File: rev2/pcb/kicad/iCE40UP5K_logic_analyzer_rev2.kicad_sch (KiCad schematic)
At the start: 151 parts, among them IC1 ICE40UP5K-SG48I, IC2 MIC5504-3.3YM5-TR, IC3 MIC5504-1.2YM5-TR, IC4 FT2232HL-TRAY, IC5 W25Q40CLSNIG, IC6 SN74LVC14ADBRE4, IC7 SN74LVC14ADBRE4, IC8 SN74LVC14ADBRE4, J1 USB B Female Connector, J2 61300611121, J3 61202021621, J4 61300821121, J5 61300821121, Q1 2N7002H6327XTSA2, Y1 830208214809

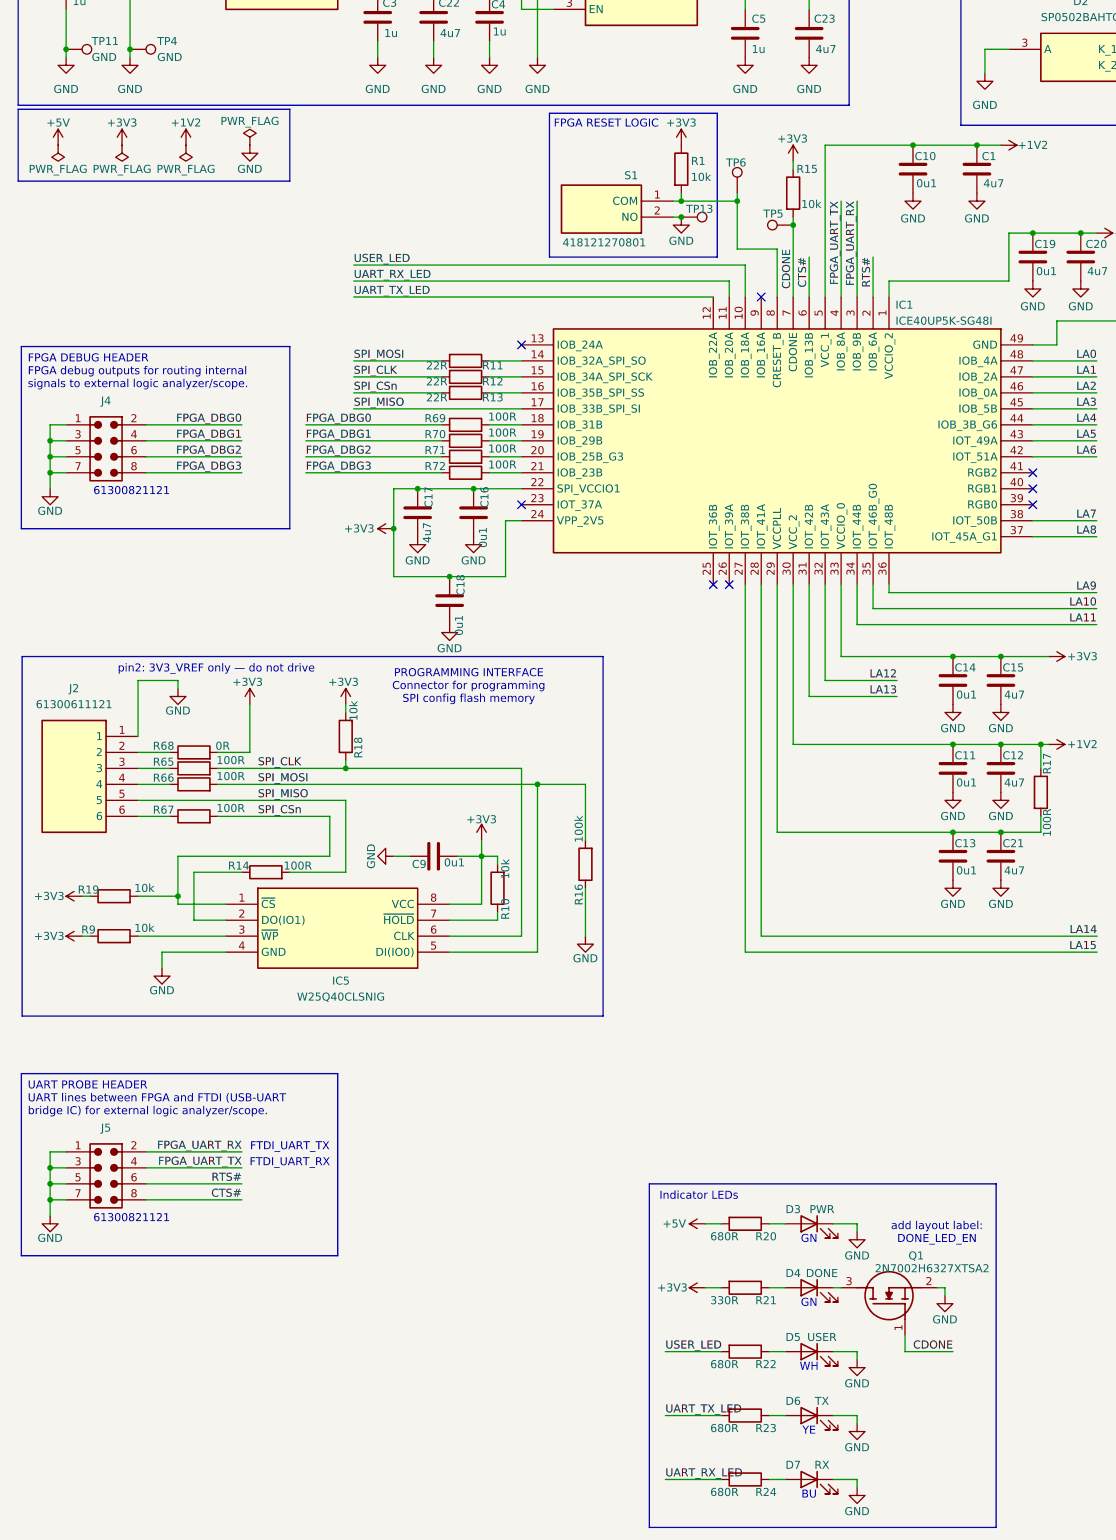
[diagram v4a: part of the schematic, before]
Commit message: Added CONFIG PROBE HEADER to schematic.
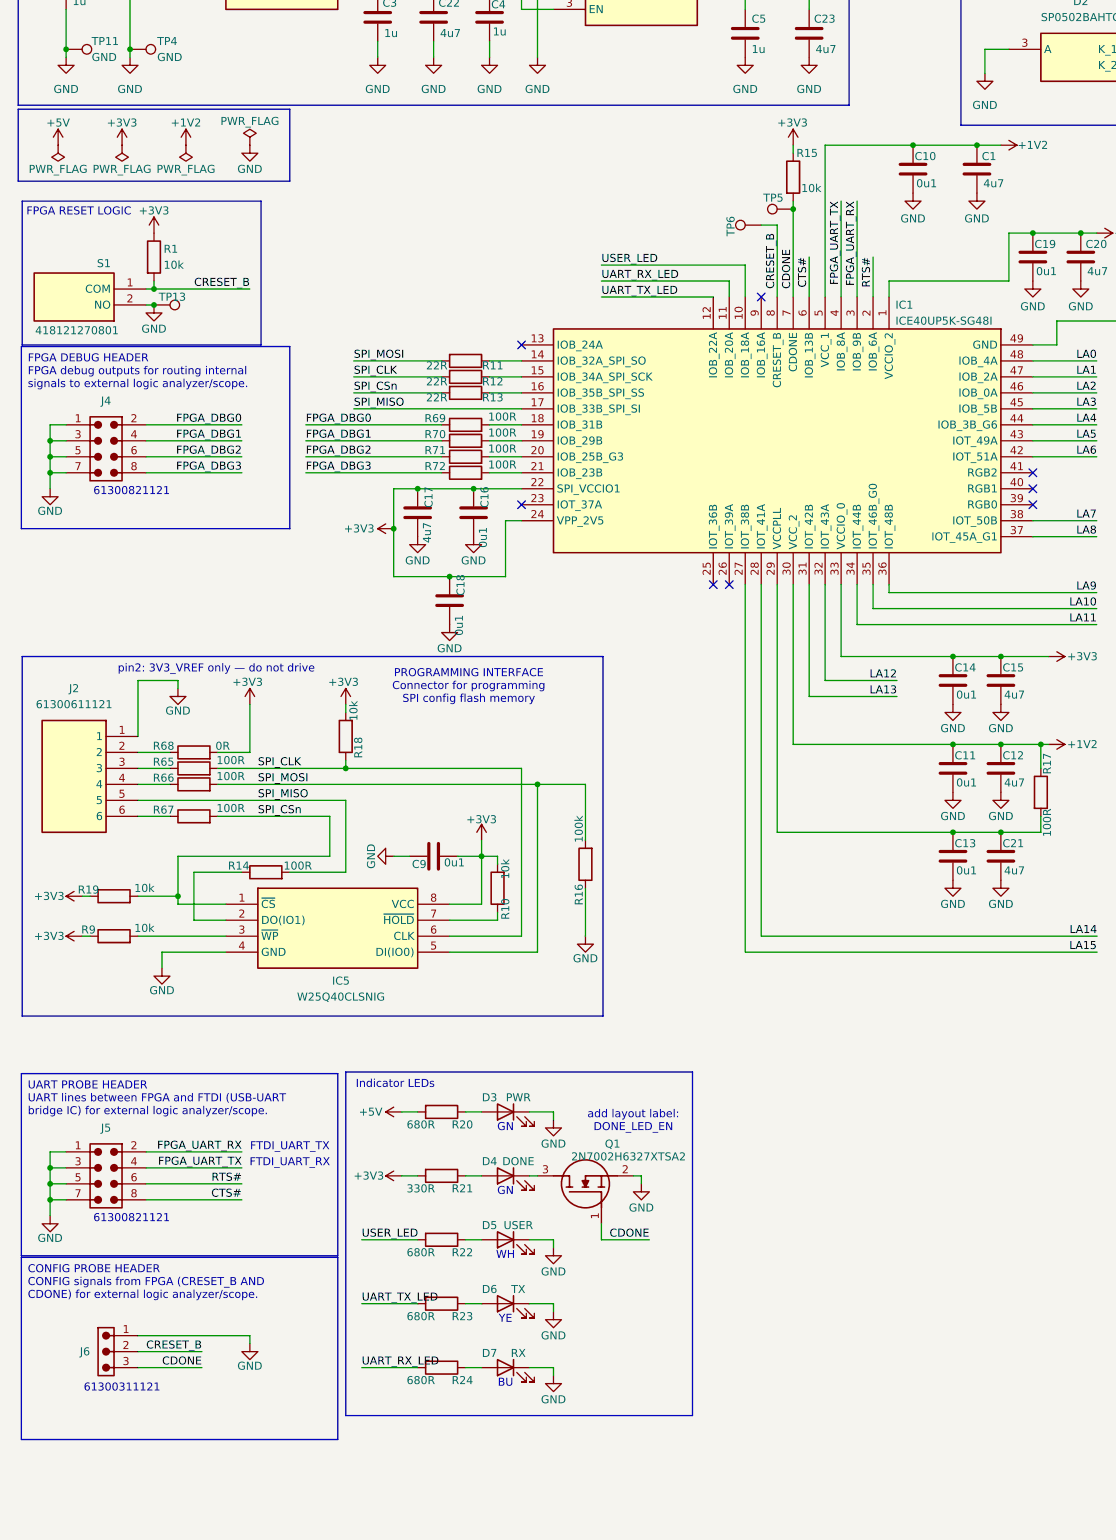
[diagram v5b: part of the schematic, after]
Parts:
- added J6: 61300311121, Connector_THT_Wurth:J_Wurth_WR-PHD_61300311121, symbol 8_pin_2x4_61300821121:61300311121
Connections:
- net CDONE: now also J6.3
- net GND: now also J6.1
- net CRESET_B: now reaches IC1.8 (CRESET_B), R1.2, S1.1 (COM), TP6.1
- net CRESET_B: now also J6.2
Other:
- note added: "61300311121"
- note added: "CONFIG PROBE HEADER CONFIG signals from FPGA (CRESET_B AND CDONE) for external logic analyzer/scope."
- moved on the sheet: D3, D4, D5, D6, D7, Q1, R1, R15, R20, R21, R22, R23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

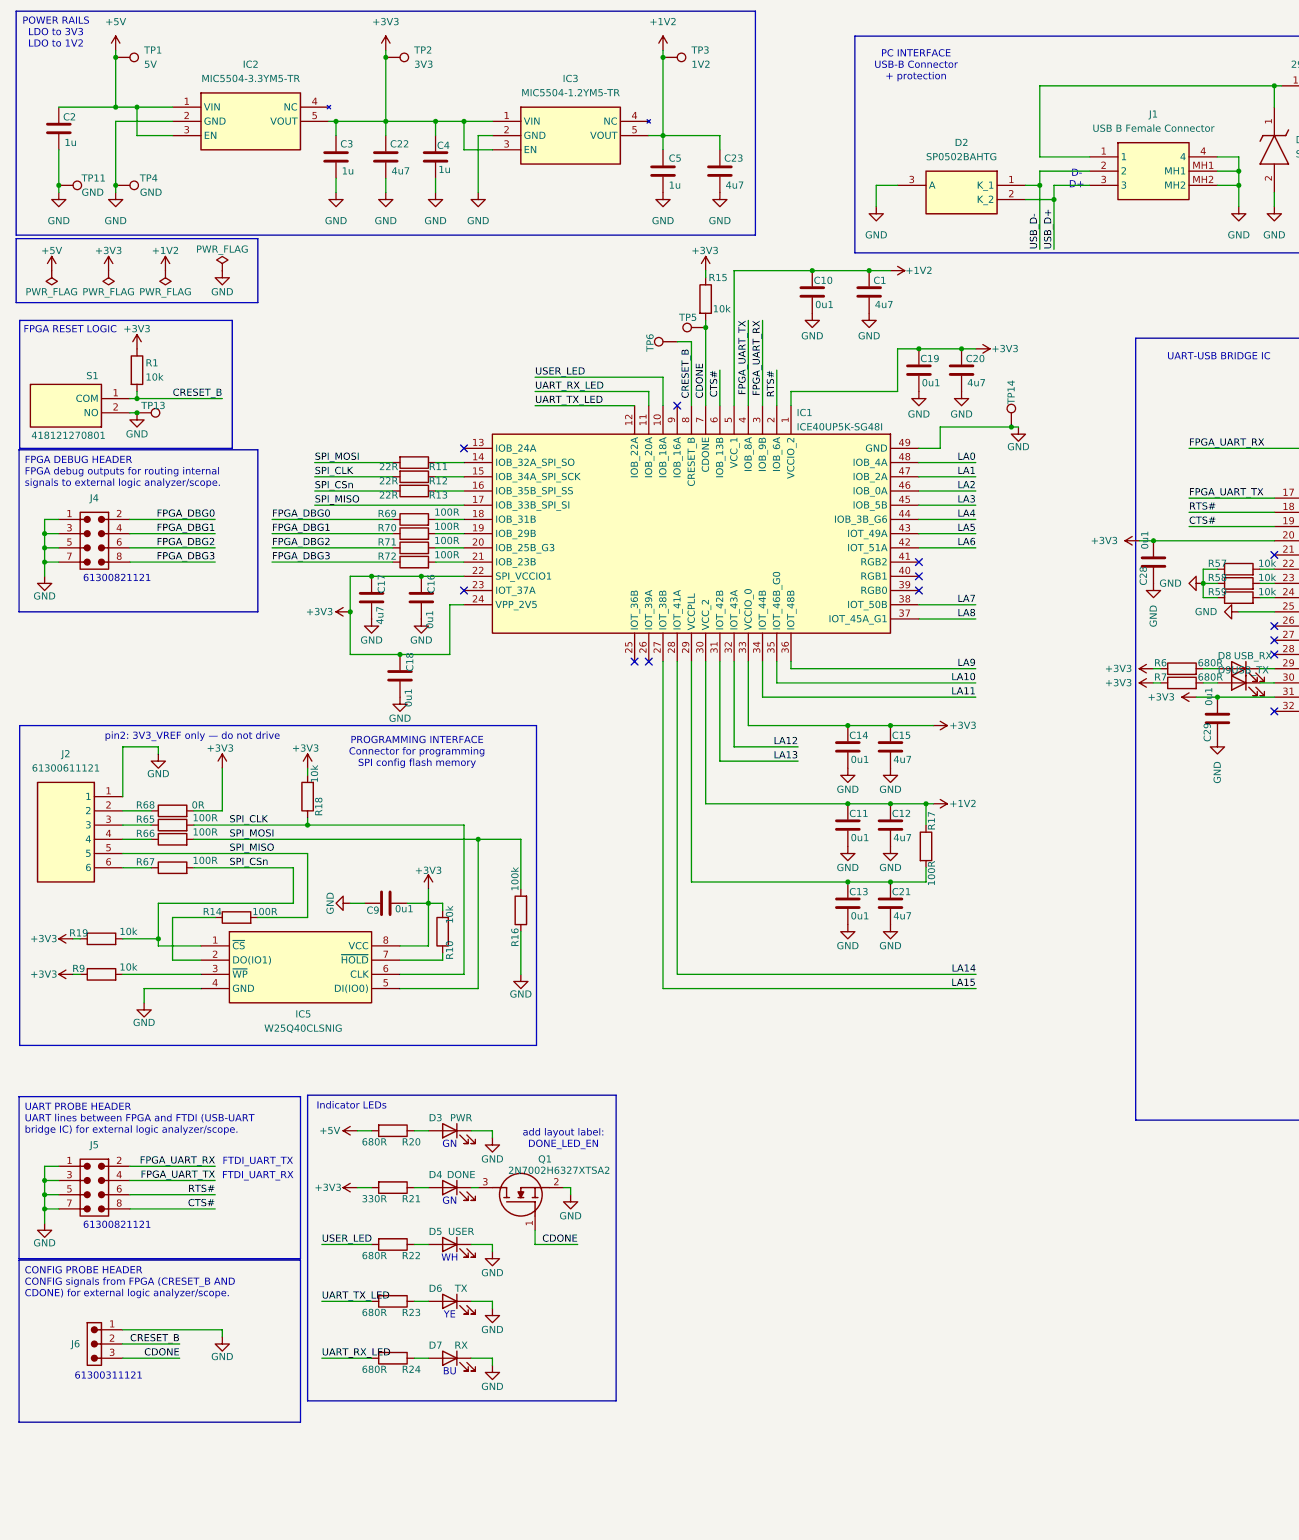
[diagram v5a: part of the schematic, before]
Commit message: Added POWER RAIL DEBUG HEADER and 0R links to LDO outputs in schematic.
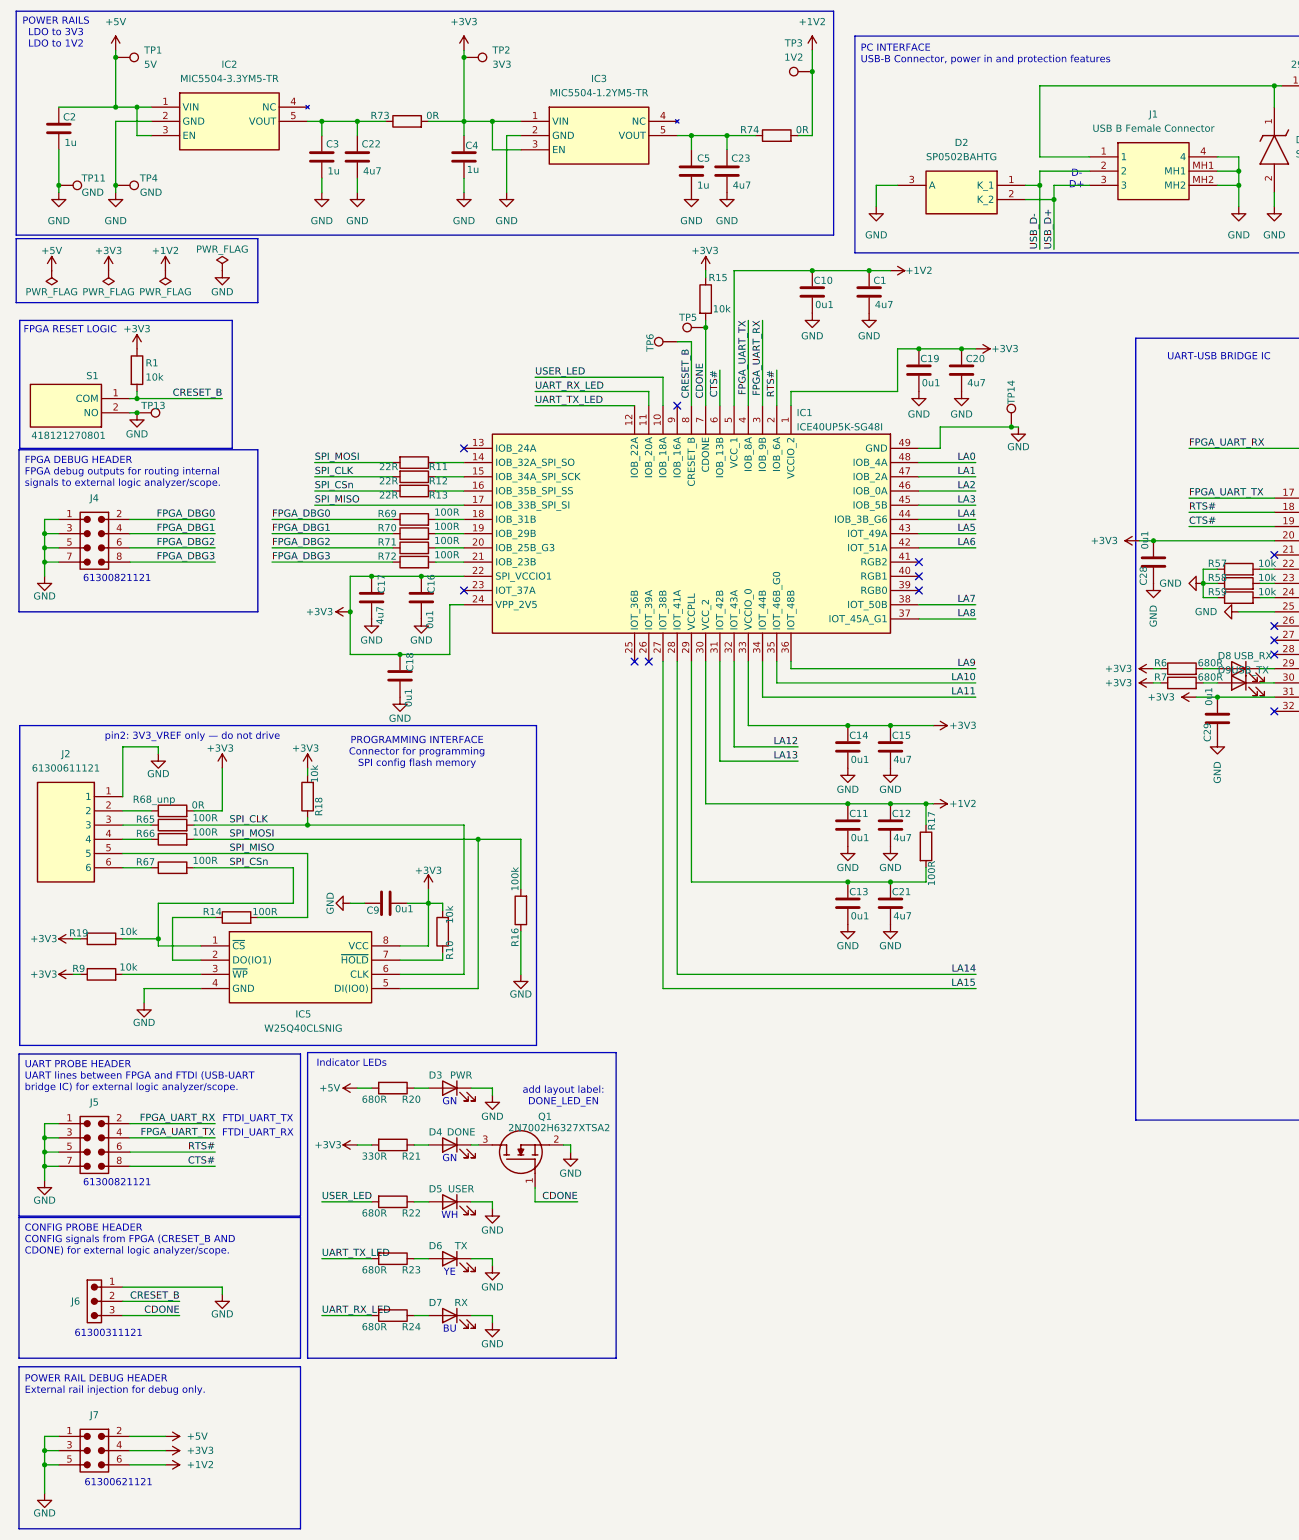
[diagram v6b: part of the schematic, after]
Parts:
- added J7: 61300621121, Connector_THT_Wurth:J_Wurth_WR-PHD_61300621121, symbol wurth_elektronik_headers:61300621121
- added R73, R74: 0R, Resistor_SMD:R_0805_2012Metric, symbol Device:R
- R68_unp: renamed from R68; footprint Resistor_SMD:R_0603_1608Metric -> Resistor_SMD:R_0805_2012Metric
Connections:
- net +1V2: now also J7.6, R74.2; no longer C23.1, C5.1, IC3.5 (VOUT)
- net +3V3: now also J7.4, R73.2; no longer C22.1, C3.1, IC2.5 (VOUT)
- net +5V: now also J7.2
- net GND: now also J7.1, J7.3, J7.5
- new net: C23.1, C5.1, IC3.5 (VOUT), R74.1
- new net: C22.1, C3.1, IC2.5 (VOUT), R73.1
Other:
- note added: "61300621121"
- note added: "PC INTERFACE USB-B Connector, power in and protection features"
- note added: "POWER RAIL DEBUG HEADER External rail injection for debug only."
- note removed: "PC INTERFACE USB-B Connector + protection"
- moved on the sheet: C22, C23, C3, C4, C5, D3, D4, D5, D6, D7, IC2, IC3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
